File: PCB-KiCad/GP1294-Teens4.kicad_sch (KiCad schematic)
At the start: 33 parts, among them Q1 ALS-PDIC144, U10 TSOP34S40F, U8 CS8421

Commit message: Fixed merge fail.
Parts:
- removed R2: 100k, Resistor_SMD:R_0603_1608Metric, symbol Device:R
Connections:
- net +3.3V: now also U1.9 (TEST)
- net F2: now also U1.28 (F-)
- net at U1.29 (F-): no longer U1.28 (F-)
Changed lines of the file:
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@@
   (junction (at 153.67 161.29) (diameter 0) (color 0 0 0 0)
   )
-  (junction (at 248.92 132.08) (diameter 0) (color 0 0 0 0)
-  )
   (junction (at 179.832 120.904) (diameter 0) (color 0 0 0 0)
   )
@@
   (junction (at 115.57 186.69) (diameter 0) (color 0 0 0 0)
   )
+  (junction (at 243.84 74.93) (diameter 0) (color 0 0 0 0)
+  )
   (junction (at 153.67 173.99) (diameter 0) (color 0 0 0 0)
   )
@@
   (junction (at 234.95 70.104) (diameter 0) (color 0 0 0 0)
   )
-  (junction (at 248.92 127) (diameter 0) (color 0 0 0 0)
-  )
   (junction (at 153.67 163.83) (diameter 0) (color 0 0 0 0)
   )
   (junction (at 173.736 35.052) (diameter 0) (color 0 0 0 0)
   )
-  (junction (at 243.84 67.31) (diameter 0) (color 0 0 0 0)
-  )
-  (junction (at 248.92 55.88) (diameter 0) (color 0 0 0 0)
-  )
   (junction (at 153.67 158.75) (diameter 0) (color 0 0 0 0)
   )
@@
   (junction (at 246.38 118.11) (diameter 0) (color 0 0 0 0)
   )
-  (junction (at 248.92 53.34) (diameter 0) (color 0 0 0 0)
-  )
   (wire (pts (xy 115.316 93.98) (xy 115.316 92.71))
     (stroke (width 0) (type default))
@@
   )
   (wire (pts (xy 250.19 53.34) (xy 248.92 53.34))
-    (stroke (width 0) (type default))
-  )
-  (wire (pts (xy 248.92 127) (xy 250.19 127))
     (stroke (width 0) (type default))
   )
@@
     (stroke (width 0) (type default))
   )
-  (wire (pts (xy 248.92 124.46) (xy 248.92 127))
+  (wire (pts (xy 248.92 124.46) (xy 248.92 138.43))
     (stroke (width 0) (type default))
   )
@@
     (stroke (width 0) (type default))
   )
-  (wire (pts (xy 250.19 60.96) (xy 248.92 60.96))
-    (stroke (width 0) (type default))
-  )
   (wire (pts (xy 186.436 113.03) (xy 184.15 113.03))
     (stroke (width 0) (type default))
@@
   )
   (wire (pts (xy 195.834 134.112) (xy 180.086 134.112))
+    (stroke (width 0) (type default))
+  )
+  (wire (pts (xy 243.84 87.63) (xy 243.84 74.93))
     (stroke (width 0) (type default))
   )
@@
     (stroke (width 0) (type default))
   )
-  (wire (pts (xy 248.92 55.88) (xy 248.92 58.42))
-    (stroke (width 0) (type default))
-  )
-  (wire (pts (xy 248.92 132.08) (xy 248.92 138.43))
-    (stroke (width 0) (type default))
-  )
   (wire (pts (xy 243.84 113.03) (xy 250.19 113.03))
     (stroke (width 0) (type default))
@@
     (stroke (width 0) (type default))
   )
-  (wire (pts (xy 243.84 67.31) (xy 243.84 87.63))
+  (wire (pts (xy 243.84 74.93) (xy 243.84 67.31))
     (stroke (width 0) (type default))
   )
@@
         (path "/3de011e3-f89b-42a8-8637-1f4c3f0867fa"
           (reference "C6") (unit 1)
-        )
-      )
-    )
-  )
-  (symbol (lib_id "Device:R") (at 241.935 71.12 180) (unit 1)
-    (in_bom yes) (on_board yes) (dnp no)
-    (property "Reference" "R2" (at 240.665 67.31 90)
-      (effects (font (size 1.27 1.27)))
-    )
-    (property "Value" "100k" (at 240.665 76.2 90)
-      (effects (font (size 1.27 1.27)))
-    )
-    (property "Footprint" "Resistor_SMD:R_0603_1608Metric" (at 243.713 71.12 90)
-      (effects (font (size 1.27 1.27)) hide)
-    )
-    (property "Datasheet" "~" (at 241.935 71.12 0)
-      (effects (font (size 1.27 1.27)) hide)
-    )
-    (property "Field4" "" (at 241.935 71.12 90)
-      (effects (font (size 1.27 1.27)) hide)
-    )
-    (pin "1")
-    (pin "2")
-    (instances
-      (project "GP1294-Teens4"
-        (path "/3de011e3-f89b-42a8-8637-1f4c3f0867fa"
-          (reference "R2") (unit 1)
         )
       )
@@
     )
     (pin "1")
+    (pin "4")
+    (pin "5")
+    (pin "7")
+    (pin "6")
     (pin "2")
     (pin "3")
-    (pin "4")
-    (pin "5")
-    (pin "6")
-    (pin "7")
     (instances
       (project "GP1294-Teens4"
@@
       (effects (font (size 1.27 1.27)) hide)
     )
-    (pin "1")
-    (pin "10")
-    (pin "11")
+    (pin "9")
     (pin "2")
     (pin "3")
     (pin "4")
+    (pin "11")
+    (pin "8")
     (pin "5")
     (pin "6")
+    (pin "10")
+    (pin "1")
     (pin "7")
-    (pin "8")
-    (pin "9")
-    (instances
-      (project "GP1294-Teens4"
+    (instances
+      (project "GP1294-Teens4"

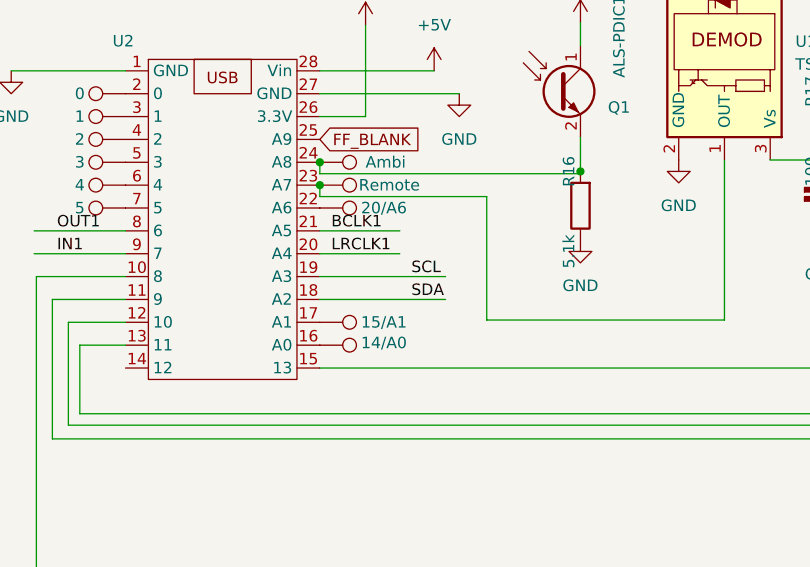
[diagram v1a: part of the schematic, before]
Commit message: Fixed i2c..
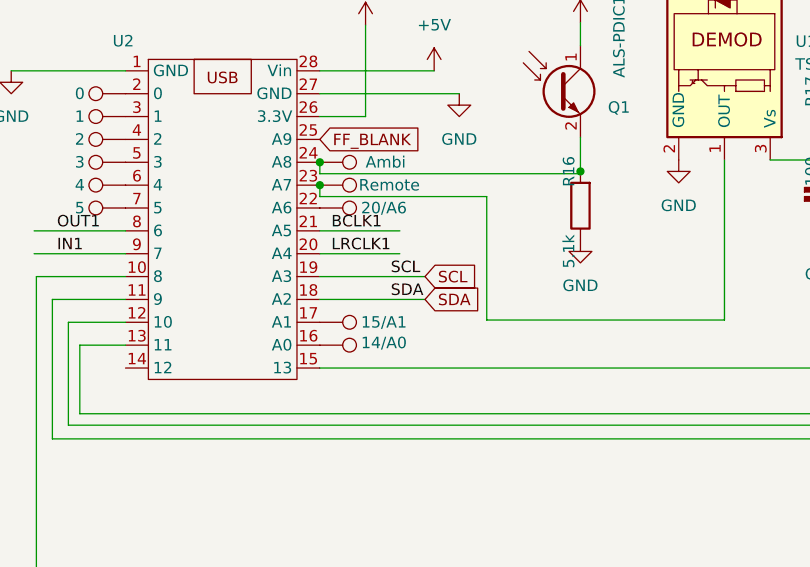
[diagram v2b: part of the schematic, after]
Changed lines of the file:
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@@
     (stroke (width 0) (type default))
   )
-  (wire (pts (xy 115.316 102.87) (xy 129.286 102.87))
+  (wire (pts (xy 115.316 102.87) (xy 127 102.87))
     (stroke (width 0) (type default))
   )
@@
     (stroke (width 0) (type default))
   )
-  (wire (pts (xy 115.316 105.41) (xy 129.286 105.41))
+  (wire (pts (xy 115.316 105.41) (xy 127 105.41))
     (stroke (width 0) (type default))
   )
@@
     (effects (font (size 1.27 1.27)) (justify left bottom))
   )
-  (label "SCL" (at 125.476 102.87 0) (fields_autoplaced)
+  (label "SCL" (at 123.19 102.87 0) (fields_autoplaced)
     (effects (font (size 1.27 1.27)) (justify left bottom))
   )
@@
     (effects (font (size 1.27 1.27)) (justify left bottom))
   )
-  (label "SDA" (at 125.476 105.41 0) (fields_autoplaced)
+  (label "SDA" (at 123.19 105.41 0) (fields_autoplaced)
     (effects (font (size 1.27 1.27)) (justify left bottom))
   )
@@
     )
   )
+  (global_label "SDA" (shape input) (at 127 105.41 0) (fields_autoplaced)
+    (effects (font (size 1.27 1.27)) (justify left))
+    (property "Intersheetrefs" "${INTERSHEET_REFS}" (at 133.5533 105.41 0)
+      (effects (font (size 1.27 1.27)) (justify left) hide)
+    )
+  )
   (global_label "FF_BLANK" (shape input) (at 115.316 87.63 0) (fields_autoplaced)
     (effects (font (size 1.27 1.27)) (justify left))
@@
     )
   )
+  (global_label "SCL" (shape input) (at 127 102.87 0) (fields_autoplaced)
+    (effects (font (size 1.27 1.27)) (justify left))
+    (property "Intersheetrefs" "${INTERSHEET_REFS}" (at 133.4928 102.87 0)
+      (effects (font (size 1.27 1.27)) (justify left) hide)
+    )
+  )

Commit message: GP1291 fixes, removed input mcu, added SRCs.
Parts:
- removed TP6: 20/A6, TestPoint:TestPoint_Pad_2.0x2.0mm, symbol Connector:TestPoint
- removed TP7: Remote, TestPoint:TestPoint_Pad_2.0x2.0mm, symbol Connector:TestPoint
- removed TP8: Ambi, TestPoint:TestPoint_Pad_2.0x2.0mm, symbol Connector:TestPoint
- removed U8: CS8421, VFDs-Library:CS8421-breakout, symbol VFDs-Library:CS8421-breakout
- added C30: 100n, Capacitor_SMD:C_0603_1608Metric_Pad1.08x0.95mm_HandSolder, symbol VFD-Power-eagle-import:C-EUC1206
- added R10, R18: 100, Resistor_SMD:R_0603_1608Metric, symbol Device:R
- added R19: 100k, Resistor_SMD:R_0603_1608Metric, symbol Device:R
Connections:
- net +3.3V: now also R19.1; no longer U1.9 (TEST)
- net BCLK1: now also U2.23 (21/A7); no longer U2.21 (A5)
- net DISP_DC: now also U2.8 (6); no longer U2.10 (8)
- net FF_BLANK: now also U2.24 (22/A8); no longer U2.25 (A9)
- net GND: now also C30.2
- net IN1: now also U2.10 (8); no longer U2.9 (7)
- net LRCLK1: now also U2.22 (20/A6); no longer U2.20 (A4)
- net OUT1: now also U2.9 (7); no longer U2.8 (6)
- net SCL: now also U2.18 (16/A2); no longer U2.19 (A3)
- net SDA: now also U2.19 (17/A3); no longer U2.18 (A2)
- net at U10.1 (OUT): now also U2.20 (18/A4); no longer U2.23 (A7)
- net at U4.15 (MCLK): now also R18.2
- net at U4.3 (MP1/MDI): now also R10.2
- net BtnCLK: now reaches TP11.1, U2.6 (4)
- net at Q1.2 (E), R16.2: now also U2.21 (19/A5); no longer U2.24 (A8)
- net BtnLAT: now reaches TP12.1, U2.5 (3)
- net BtnSIN: now reaches TP10.1, U2.7 (5)
- new net: C30.1, R19.2, U1.9 (TEST)
- new net MCLK: U2.25 (23/A9)
- new net SRC/MCLK_DSP: R18.1
- new net SRC/To_DSP: R10.1
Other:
- added sheet SRC (SRC2x.kicad_sch)
- note added: "AMBI"
- note added: "D_DC_ONLY_OLED"
- note added: "D_RESET"
- note added: "FreeDSP Connector"
- note added: "REMOTE"
- note added: "const byte pinFFBlank = 23; //=A9; const byte pinAmbi = 22; // ambient light, analog value const byte pinRemote = 21; // LIRC input pin, sensor=4838"
- note added: "pinSLat 3 pinSCLK 4 pinSIN 5"
- note removed: "CS8421 I2S IIS Sampling Rate Conversion Module Configure as SlaveIn SlaveOut ! MSEL pin 15 -> 1k to GND SAIF pin 19 -> 1k to GND (input i2s anything) SAOF pin 18 -> 4k to GND (output i2s 24bit)"
- moved on the sheet: C15, C6, C9, Q1, R11, R12, R16, R17, R2, R3, R7, R8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
